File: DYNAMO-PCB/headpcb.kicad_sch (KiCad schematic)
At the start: 15 parts, among them J10 Conn_01x03_Pin, J11 Conn_01x03_Pin, J12 Conn_01x03_Pin, J33 Conn_02x05_Counter_Clockwise, J5 Conn_01x02_Pin, J6 Conn_01x03_Pin, J7 Conn_01x08_Socket, J8 Conn_01x03_Pin, J9 Conn_01x03_Pin

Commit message: schematic wip
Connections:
- net GND: now also J10.1 (Pin_1), J11.1 (Pin_1), J5.1 (Pin_1), J6.1 (Pin_1), J8.1 (Pin_1), J9.1 (Pin_1); no longer J10.3 (Pin_3), J11.3 (Pin_3), J12.3 (Pin_3), J5.2 (Pin_2), J6.3 (Pin_3), J8.3 (Pin_3), J9.3 (Pin_3)
- net at C2.1, C3.1, C4.1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: now also J11.3 (Pin_3), J12.1 (Pin_1), J12.3 (Pin_3), J5.2 (Pin_2); no longer J11.2 (Pin_2), J12.2 (Pin_2), J5.1 (Pin_1)
- net at R3.2: now also J12.2 (Pin_2); no longer J12.1 (Pin_1)
- net at J33.3 (Pin_3): now also J10.3 (Pin_3); no longer J10.1 (Pin_1)
- net at R2.2: now also J11.2 (Pin_2); no longer J11.1 (Pin_1)
- net at J33.6 (Pin_6): now also J9.3 (Pin_3); no longer J9.1 (Pin_1)
- net at J33.7 (Pin_7): now also J8.3 (Pin_3); no longer J8.1 (Pin_1)
- net at J33.8 (Pin_8): now also J6.3 (Pin_3); no longer J6.1 (Pin_1)
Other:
- moved on the sheet: J6, J8

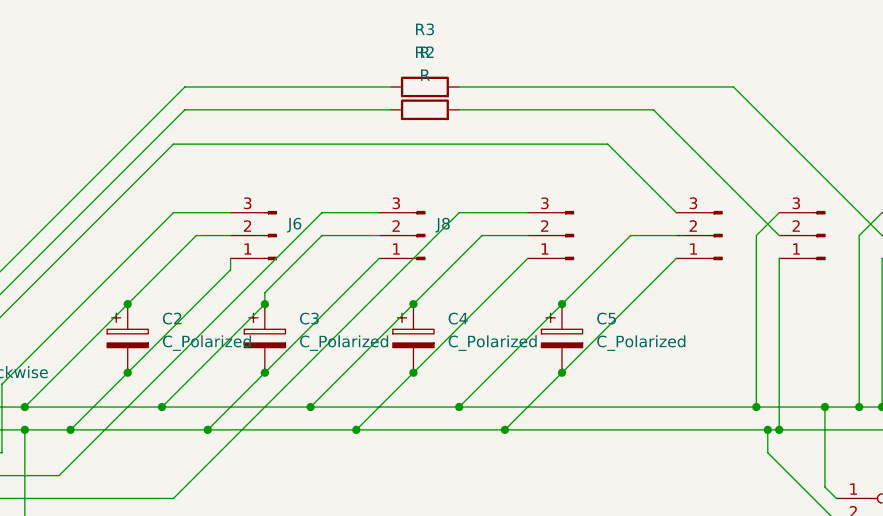
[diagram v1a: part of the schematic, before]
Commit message: schematic complete (pre-ERC)
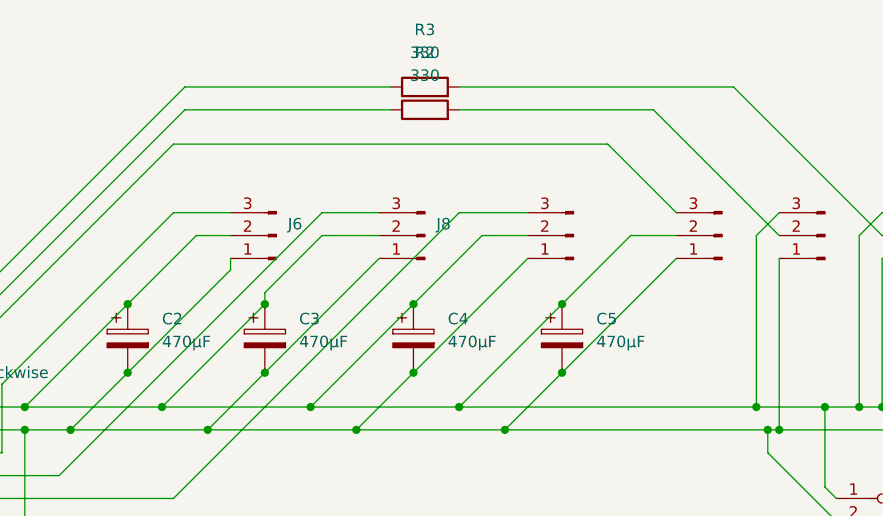
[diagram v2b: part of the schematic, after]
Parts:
- C2, C3, C4, C5: value C_Polarized -> 470µF
- R2, R3: value R -> 330
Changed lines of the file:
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@@
 			)
 		)
-		(property "Value" "R"
+		(property "Value" "330"
 			(at 147.32 55.88 90)
 			(effects
@@
 			)
 		)
-		(property "Value" "C_Polarized"
+		(property "Value" "470µF"
 			(at 118.11 88.0109 0)
 			(effects
@@
 			)
 		)
-		(property "Value" "C_Polarized"
+		(property "Value" "470µF"
 			(at 149.86 88.0109 0)
 			(effects
@@
 			)
 		)
-		(property "Value" "C_Polarized"
+		(property "Value" "470µF"
 			(at 166.37 88.0109 0)
 			(effects
@@
 			)
 		)
-		(property "Value" "C_Polarized"
+		(property "Value" "470µF"
 			(at 133.35 88.0109 0)
 			(effects
@@
 			)
 		)
-		(property "Value" "R"
+		(property "Value" "330"
 			(at 147.32 58.42 90)
 			(effects

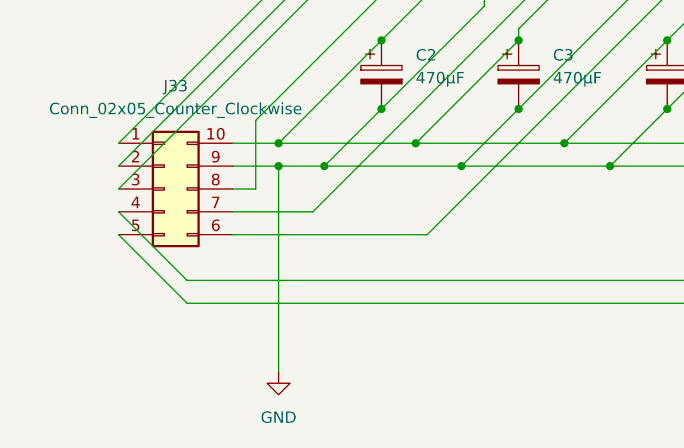
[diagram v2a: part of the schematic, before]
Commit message: fix erc errors
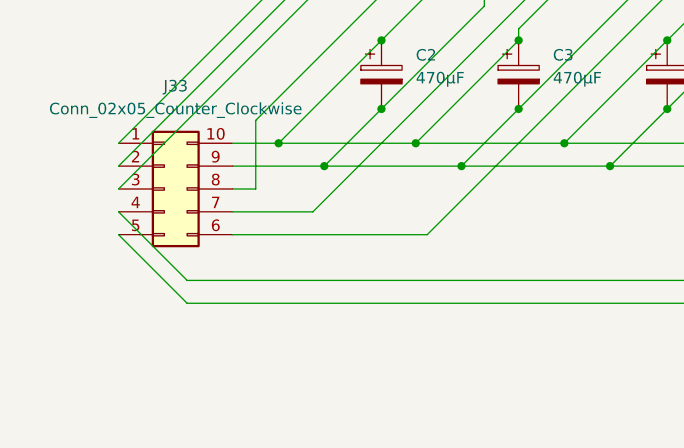
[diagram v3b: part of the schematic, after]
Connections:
- net GND: no longer names the net of C2.2, C3.2, C4.2, C5.2, J10.1 (Pin_1), J11.1 (Pin_1), J33.9 (Pin_9), J5.1 (Pin_1), J6.1 (Pin_1), J7.2 (Pin_2), J8.1 (Pin_1), J9.1 (Pin_1)
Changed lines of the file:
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@@
-	)
-	(junction
-		(at 102.87 97.79)
-		(diameter 0)
-		(color 0 0 0 0)
 	)
 	(junction
@@
 	(wire
 		(pts
-			(xy 102.87 97.79) (xy 102.87 120.65)
-		)
-		(stroke
-			(width 0)
-			(type default)
-		)
-	)
-	(wire
-		(pts
 			(xy 92.71 113.03) (xy 85.09 105.41)
 		)
@@
 	(wire
 		(pts
-			(xy 102.87 97.79) (xy 107.95 97.79)
+			(xy 97.79 97.79) (xy 107.95 97.79)
 		)
 		(stroke
@@
 		(pts
 			(xy 198.12 78.74) (xy 198.12 95.25)
-		)
-		(stroke
-			(width 0)
-			(type default)
-		)
-	)
-	(wire
-		(pts
-			(xy 97.79 97.79) (xy 102.87 97.79)
 		)
 		(stroke
@@
 					(unit 1)
 				)
-			)
-		)
-	)
-	(symbol
-		(lib_id "power:GND")
-		(at 102.87 120.65 0)
-		(unit 1)
-		(exclude_from_sim no)
-		(in_bom yes)
-		(on_board yes)
-		(dnp no)
-		(fields_autoplaced yes)
-		(property "Reference" "#PWR01"
-			(at 102.87 127 0)
-			(effects
-				(font
-					(size 1.27 1.27)
-				)
-				(hide yes)
-			)
-		)
-		(property "Value" "GND"
-			(at 102.87 125.73 0)
-			(effects
-				(font
-					(size 1.27 1.27)
-				)
-			)
-		)
-		(property "Footprint" ""
-			(at 102.87 120.65 0)
-			(effects
-				(font
-					(size 1.27 1.27)
-				)
-				(hide yes)
-			)
-		)
-		(property "Datasheet" ""
-			(at 102.87 120.65 0)
-			(effects
-				(font
-					(size 1.27 1.27)
-				)
-				(hide yes)
-			)
-		)
-		(property "Description" "Power symbol creates a global label with name \"GND\" , ground"
-			(at 102.87 120.65 0)
-			(effects
-				(font
-					(size 1.27 1.27)
-				)
-				(hide yes)
-			)
-		)
-		(pin "1"
-		)
-		(instances
-			(project ""
-				(path "/2ca9dd43-411d-4cc5-8a4b-ed00d72bae91/8fd238d6-8885-491d-831e-5a6be755c492"
-					(reference "#PWR01")
-					(unit 1)
-				)

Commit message: placement wip
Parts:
- C2, C3, C4, C5: footprint Capacitor_THT:CP_Radial_D10.0mm_P5.00mm -> Capacitor_THT:CP_Radial_D8.0mm_P3.50mm
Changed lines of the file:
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@@
 			)
 		)
-		(property "Footprint" "Capacitor_THT:CP_Radial_D10.0mm_P5.00mm"
+		(property "Footprint" "Capacitor_THT:CP_Radial_D8.0mm_P3.50mm"
 			(at 115.2652 91.44 0)
 			(effects
@@
 			)
 		)
-		(property "Footprint" "Capacitor_THT:CP_Radial_D10.0mm_P5.00mm"
+		(property "Footprint" "Capacitor_THT:CP_Radial_D8.0mm_P3.50mm"
 			(at 147.0152 91.44 0)
 			(effects
@@
 			)
 		)
-		(property "Footprint" "Capacitor_THT:CP_Radial_D10.0mm_P5.00mm"
+		(property "Footprint" "Capacitor_THT:CP_Radial_D8.0mm_P3.50mm"
 			(at 163.5252 91.44 0)
 			(effects
@@
 			)
 		)
-		(property "Footprint" "Capacitor_THT:CP_Radial_D10.0mm_P5.00mm"
+		(property "Footprint" "Capacitor_THT:CP_Radial_D8.0mm_P3.50mm"
 			(at 130.5052 91.44 0)
 			(effects
